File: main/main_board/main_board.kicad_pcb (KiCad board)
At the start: 4 copper layers, 426.7 x 242.2 mm, 58 parts, among them J7 SCKB, J8 SCKA, J9 MCLK, P2 my_pcie_8x, P3 my_pcie_8x, P4 my_pcie_8x, P5 my_pcie_8x, P6 my_pcie_8x, U11 MCP1755S-3302E/DB, U12 FIN1047, U13 DS90LV048, U14 74LVC541A, U15 FIN1047, U16 FIN1047, U17 FIN1047

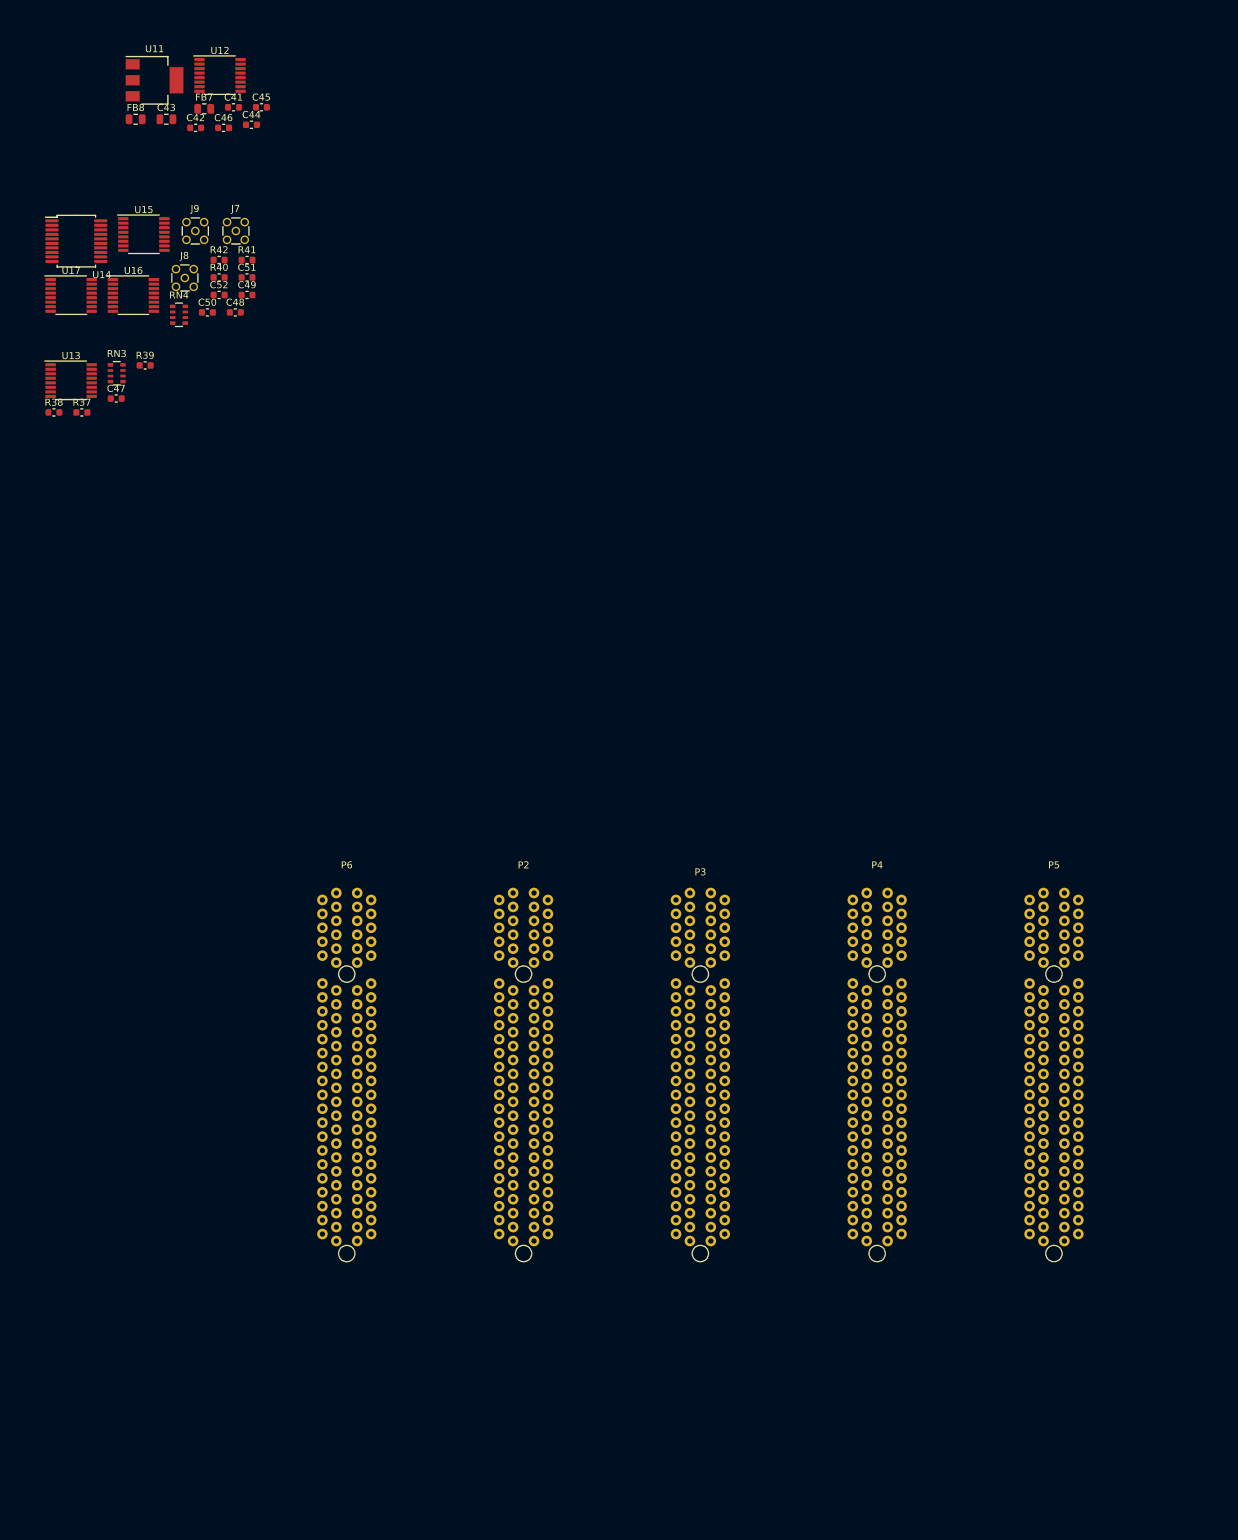
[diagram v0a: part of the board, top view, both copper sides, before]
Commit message: A bunch of thinking about RFI and ESD, and some testing.  Mostly reflected in notebook.txt. Also another more explicit round of consideration of box-level grounding and power distribution, because this affects the power conditioning on the main board.  Power nets on the main board are mostly captured.  I added supply decoupling at each plugin slot.
in_filter.sxsch: added simulation of ESD, use vendor models for TVS diode and ferrite.

power_budget.xlsx: get rid of sheets for the input boards not implemented.  Add sheet for
the main board and carry over data from the input board sheet.
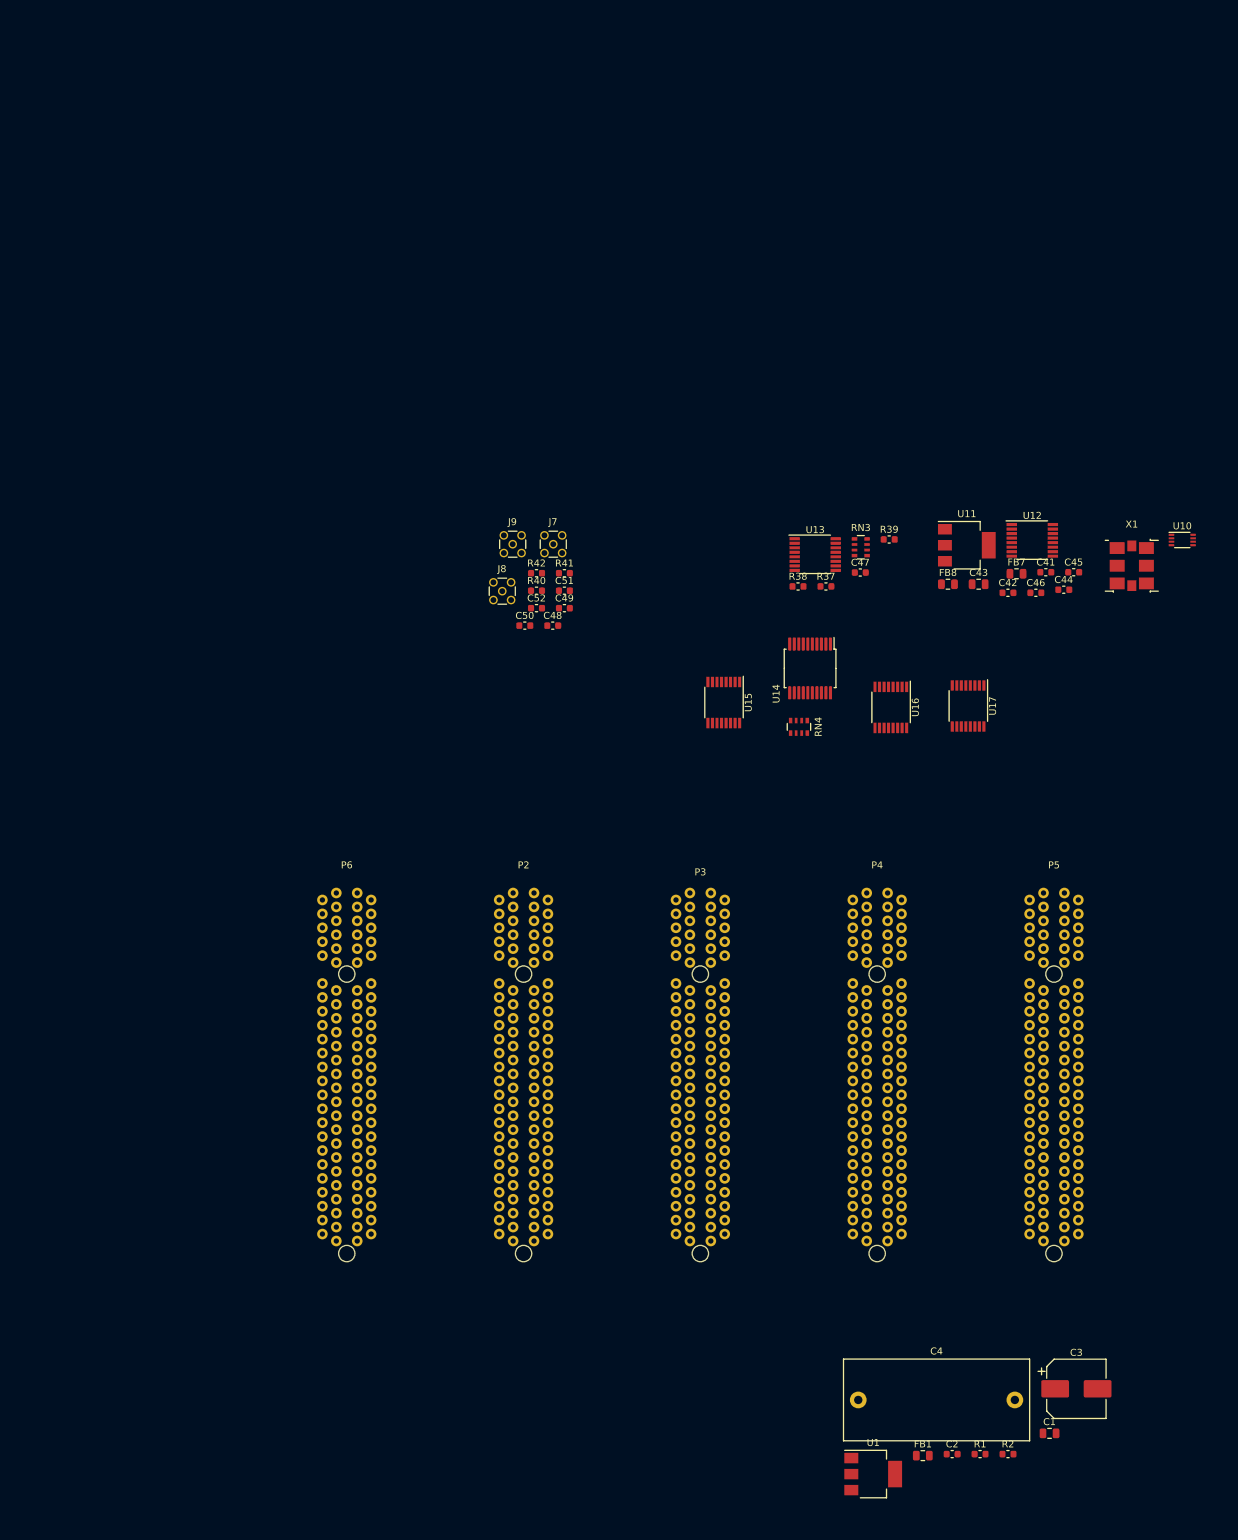
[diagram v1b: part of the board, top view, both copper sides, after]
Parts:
- added C1: 1uF, Capacitor_SMD:C_0805_2012Metric, F.Cu at (419.2, 243.0)
- added C2: 10uF, Capacitor_SMD:C_0603_1608Metric, F.Cu at (405.2, 246.0)
- added C3: 330uF, Capacitor_SMD:CP_Elec_8x6.7, F.Cu at (423.1, 236.6)
- added C4: 22 uF, Capacitor_THT:C_Rect_L26.5mm_W11.5mm_P22.50mm_MKS4, F.Cu at (391.7, 238.2)
- added FB1: 21 Ohm, Inductor_SMD:L_0805_2012Metric, F.Cu at (401.0, 246.2)
- added R1: 1K, Resistor_SMD:R_0603_1608Metric, F.Cu at (409.2, 246.0)
- added R2: 200, Resistor_SMD:R_0603_1608Metric, F.Cu at (413.2, 246.0)
- added U1: NCP1117STAT3G, Package_TO_SOT_SMD:SOT-223, F.Cu at (393.9, 248.8)
- added U10: 74AUP1G74, Package_SO:VSSOP-8_2.3x2mm_P0.5mm, F.Cu at (438.3, 114.7)
- added X1: Si570, input:QFN-8_5x7_Pitch2.54mm, F.Cu at (431.0, 118.3)
- moved U17 141.7 mm to (407.5, 138.5), turned to 270 degrees
- moved C41 134.5 mm to (418.7, 119.3)
- moved C42 134.5 mm to (413.2, 122.2)
- moved U12 134.5 mm to (416.7, 114.7)
- moved C43 134.5 mm to (409.0, 121.0)
- moved C44 134.5 mm to (421.2, 121.8)
- moved C45 134.5 mm to (422.7, 119.3)
- moved C46 134.5 mm to (417.2, 122.2)
- moved FB7 134.5 mm to (414.5, 119.5)
- moved FB8 134.5 mm to (404.6, 121.0)
- moved U11 134.5 mm to (407.3, 115.4)
- moved U16 123.9 mm to (396.4, 138.7), turned to 270 degrees
- moved U14 122.0 mm to (384.8, 133.1), turned to 270 degrees
- moved R39 109.8 mm to (396.2, 114.6)
- moved U13 109.8 mm to (385.5, 116.7)
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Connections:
- net /output_slot/MCLK+ renamed DOUT2+
- net /output_slot/MCLK- renamed DOUT2-
- net /output_slot/SCKA+ renamed DOUT1+
- net /output_slot/SCKA- renamed DOUT1-
- net /output_slot/SCKB+ renamed /output_slot/SYSCLK+
- net /output_slot/SCKB- renamed /output_slot/SYSCLK-
- net /output_slot/SDOA1+ renamed DFB1+
- net /output_slot/SDOA1- renamed DFB1-
- net /output_slot/SDOA2+ renamed DFB3+
- net /output_slot/SDOA2- renamed DFB3-
- net /output_slot/SDOA3+ renamed DFB4+
- net /output_slot/SDOA3- renamed DFB4-
- net /output_slot/SDOB1+ renamed DFB2+
- net /output_slot/SDOB1- renamed DFB2-
- net Net-(P6-PadA3) renamed DOUTL1
- net Net-(P6-PadA7) renamed DOUTL3
- net Net-(P6-PadA8) renamed DOUTL5
- net Net-(P6-PadB25) renamed DOUT3-
- net Net-(P6-PadB3) renamed DOUTL2
- net Net-(P6-PadB7) renamed LDOUT4
- net Net-(P6-PadB8) renamed DOUTL6
- P6 pad A25: Net-(P6-PadA25) -> GND
- P6 pad A26: GND -> DOUT4+
- P6 pad A27: Net-(P6-PadA27) -> DOUT4-
- P6 pad A30: GNDA -> DOUT5+
- P6 pad A31: GNDA -> DOUT5-
- P6 pad A34: GNDA -> DOUT7+
- P6 pad A35: GNDA -> DOUT7-
- P6 pad A36: +5VANA -> GNDA
- P6 pad A37: +10V -> GNDA
- P6 pad A38: +10V -> GNDA
- P6 pad A39: -6V -> GNDA
- P6 pad A40: -6V -> GNDA
- P6 pad A41: GNDA -> +5VANA
- P6 pad A42: VREF+ -> +10V
- P6 pad A43: VREF- -> -6V
- P6 pad A45: Net-(P6-PadA45) -> VREF+
- P6 pad A46: Net-(P6-PadA46) -> VREF-
- P6 pad B24: GND -> DOUT3+
- P6 pad B27: Net-(P6-PadB27) -> GND
- P6 pad B28: GND -> DOUT4+
- P6 pad B29: GNDA -> DOUT4-
- P6 pad B32: GNDA -> DOUT6+
- P6 pad B33: GNDA -> DOUT6-
- P6 pad B36: +5VANA -> DOUT8+
- P6 pad B37: +10V -> DOUT8-
- P6 pad B38: +10V -> GNDA
- P6 pad B39: -6V -> GNDA
- P6 pad B40: -6V -> GNDA
- P6 pad B41: GNDA -> +5VANA
- P6 pad B42: GNDA -> +10V
- P6 pad B43: GNDA -> -6V
- P6 pad B45: Net-(P6-PadB45) -> GNDA
- P6 pad B46: Net-(P6-PadB46) -> GNDA
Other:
- board text added: "Microzed footprint"

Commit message: Mostly work on hooking in the Microzed using kipart symbols and a footprint. Also added 2.5V VCCIO regulator.
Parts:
- added C1: 1uF, Capacitor_SMD:C_0805_2012Metric, F.Cu at (369.9, 236.5)
- added C10: 1uF, Capacitor_SMD:C_0805_2012Metric, F.Cu at (262.7, 65.6)
- added C11: 1uF, Capacitor_SMD:C_0805_2012Metric, F.Cu at (279.1, 81.1)
- added C12: 330uF, Capacitor_SMD:CP_Elec_8x6.7, F.Cu at (338.5, 150.8)
- added C13: 330uF, Capacitor_SMD:CP_Elec_8x6.7, F.Cu at (321.5, 151.4)
- added C14: 1uF, Capacitor_SMD:C_0805_2012Metric, F.Cu at (279.7, 84.0)
- added C15: 1uF, Capacitor_SMD:C_0805_2012Metric, F.Cu at (279.1, 78.1)
- added C16: 1uF, Capacitor_SMD:C_0805_2012Metric, F.Cu at (275.3, 85.0)
- added C17: 1uF, Capacitor_SMD:C_0805_2012Metric, F.Cu at (279.1, 75.2)
- added C18: 1uF, Capacitor_SMD:C_0805_2012Metric, F.Cu at (275.3, 88.0)
- added C19: 330uF, Capacitor_SMD:CP_Elec_8x6.7, F.Cu at (327.7, 51.6)
- added C2: 1uF, Capacitor_SMD:C_0805_2012Metric, F.Cu at (341.3, 251.6)
- added C20: 330uF, Capacitor_SMD:CP_Elec_8x6.7, F.Cu at (321.1, 137.4)
- added C21: 330uF, Capacitor_SMD:CP_Elec_8x6.7, F.Cu at (354.9, 150.9)
- added C22: 10uF, Capacitor_SMD:C_0603_1608Metric, F.Cu at (305.1, 77.6)
- added C23: 10uF, Capacitor_SMD:C_0603_1608Metric, F.Cu at (307.7, 72.5)
- added C24: 1uF, Capacitor_SMD:C_0805_2012Metric, F.Cu at (340.9, 223.7)
- added C25: 1uF, Capacitor_SMD:C_0805_2012Metric, F.Cu at (345.3, 223.7)
- added C26: 1uF, Capacitor_SMD:C_0805_2012Metric, F.Cu at (345.3, 226.7)
- added C27: 1uF, Capacitor_SMD:C_0805_2012Metric, F.Cu at (340.9, 226.7)
- added C28: 1uF, Capacitor_SMD:C_0805_2012Metric, F.Cu at (371.6, 227.7)
- added C29: 1uF, Capacitor_SMD:C_0805_2012Metric, F.Cu at (371.6, 224.7)
- added C3: bulk >=16V, Capacitor_SMD:C_1210_3225Metric, F.Cu at (364.9, 237.1)
- added C30: 1uF, Capacitor_SMD:C_0805_2012Metric, F.Cu at (367.2, 227.7)
- added C31: 1uF, Capacitor_SMD:C_0805_2012Metric, F.Cu at (367.2, 224.7)
- added C32: 1uF, Capacitor_SMD:C_0805_2012Metric, F.Cu at (392.8, 228.2)
- added C33: 1uF, Capacitor_SMD:C_0805_2012Metric, F.Cu at (392.8, 225.2)
- added C34: 1uF, Capacitor_SMD:C_0805_2012Metric, F.Cu at (388.3, 228.2)
- added C35: 1uF, Capacitor_SMD:C_0805_2012Metric, F.Cu at (388.3, 225.2)
- added C36: 1uF, Capacitor_SMD:C_0805_2012Metric, F.Cu at (423.0, 227.9)
- added C37: 1uF, Capacitor_SMD:C_0805_2012Metric, F.Cu at (423.0, 225.0)
- added C38: 1uF, Capacitor_SMD:C_0805_2012Metric, F.Cu at (418.6, 227.9)
- added C39: 1uF, Capacitor_SMD:C_0805_2012Metric, F.Cu at (418.6, 225.0)
- added C40: 1uF, Capacitor_SMD:C_0805_2012Metric, F.Cu at (315.3, 226.3)
- added C43: 1uF, Capacitor_SMD:C_0805_2012Metric, F.Cu at (319.7, 223.4)
- added C45: 1uF, Capacitor_SMD:C_0805_2012Metric, F.Cu at (315.3, 223.4)
- added C47: 1uF, Capacitor_SMD:C_0805_2012Metric, F.Cu at (306.6, 84.4)
- added C5: 3.3 uF, Capacitor_THT:C_Rect_L13.0mm_W6.0mm_P10.00mm_FKS3_FKP3_MKS4, F.Cu at (341.4, 246.3)
- added C53: 1uF, Capacitor_SMD:C_0805_2012Metric, F.Cu at (319.7, 226.3)
- added C54: 100nF, Capacitor_SMD:C_0603_1608Metric, F.Cu at (454.0, 141.3)
- added C55: 10uF, Capacitor_SMD:C_0603_1608Metric, F.Cu at (328.3, 67.1)
- added C56: 10uF, Capacitor_SMD:C_0603_1608Metric, F.Cu at (330.5, 73.9)
- added C6: 47uF, Capacitor_SMD:C_1210_3225Metric, F.Cu at (356.4, 250.0)
- added C7: 1uF, Capacitor_SMD:C_0805_2012Metric, F.Cu at (350.1, 251.6)
- added C8: OPT, Capacitor_SMD:C_0603_1608Metric, F.Cu at (364.1, 244.7)
- added C9: 47uF, Capacitor_SMD:C_1210_3225Metric, F.Cu at (364.9, 241.3)
- added D1: 10V (standoff), Diode_SMD:D_SMA, F.Cu at (262.2, 76.2)
- added D2: 10V (standoff), Diode_SMD:D_SMA, F.Cu at (272.4, 69.7)
- added D3: 5V (standoff), Diode_SMD:D_SMA, F.Cu at (262.5, 82.9)
- added FB2: 2K Ohm, Inductor_SMD:L_0805_2012Metric, F.Cu at (369.9, 239.4)
- added FB3: 1.2 A, Inductor_SMD:L_0805_2012Metric, F.Cu at (272.5, 61.4)
- added J1: Conn_02x08_Odd_Even, Connector_PinHeader_2.54mm:PinHeader_2x08_P2.54mm_Vertical, F.Cu at (248.6, 71.6)
- added J2: MCLK, Connector_Coaxial:MMCX_Molex_73415-1471_Vertical, F.Cu at (429.7, 129.7)
- added R1: 10, Resistor_SMD:R_0603_1608Metric, F.Cu at (365.3, 249.7)
- added R10: 100, Resistor_SMD:R_0603_1608Metric, F.Cu at (449.8, 146.1)
- added R11: 100, Resistor_SMD:R_0603_1608Metric, F.Cu at (440.9, 148.1)
- added R2: 10, Resistor_SMD:R_0603_1608Metric, F.Cu at (365.3, 247.2)
- added R3: 40K, Resistor_SMD:R_0603_1608Metric, F.Cu at (368.1, 244.7)
- added R4: 10, Resistor_SMD:R_0603_1608Metric, F.Cu at (361.2, 251.7)
- added R5: 0, Resistor_SMD:R_0603_1608Metric, F.Cu at (369.7, 242.2)
- added R6: 0, Resistor_SMD:R_0603_1608Metric, F.Cu at (361.2, 249.2)
- added R7: 1K, Resistor_SMD:R_0603_1608Metric, F.Cu at (434.6, 130.6)
- added R8: 33, Resistor_SMD:R_0603_1608Metric, F.Cu at (434.6, 128.1)
- added R9: 100, Resistor_SMD:R_0603_1608Metric, F.Cu at (444.9, 148.1)
- added RN1: 33, Resistor_SMD:R_Array_Convex_4x0603, F.Cu at (449.9, 142.4)
- added U2: OPA209, Package_SO:SOIC-8_3.9x4.9mm_P1.27mm, F.Cu at (357.9, 244.7)
- added U3: MCP1755S-3302E/DB, Package_TO_SOT_SMD:SOT-223-3_TabPin2, F.Cu at (294.9, 74.4)
- added U4: MCP1755S-3302E/DB, Package_TO_SOT_SMD:SOT-223-3_TabPin2, F.Cu at (295.5, 85.9)
- added U5: DS90LV048, Package_SO:TSSOP-16_4.4x5mm_P0.65mm, F.Cu at (443.3, 143.5)
- added U6: AP3761C-25SP, Package_SO:SOIC-8-1EP_3.9x4.9mm_P1.27mm_EP2.41x3.3mm_ThermalVias, F.Cu at (330.5, 62.6)
- added X1: MicroZed, main_board:Microzed, F.Cu at (391.5, 72.4)
- C4: value 22 uF -> 3.3 uF; footprint Capacitor_THT:C_Rect_L26.5mm_W11.5mm_P22.50mm_MKS4 -> Capacitor_THT:C_Rect_L13.0mm_W6.0mm_P10.00mm_FKS3_FKP3_MKS4
- FB1: value 21 Ohm -> 2K Ohm
- U1: value NCP1117STAT3G -> MAX6220ASA-5.0+; footprint Package_TO_SOT_SMD:SOT-223 -> Package_SO:SOIC-8_3.9x4.9mm_P1.27mm
- moved FB1 55.6 mm to (345.7, 251.6)
- moved C4 50.4 mm to (341.4, 238.8)
- moved U1 37.5 mm to (357.9, 238.2)
- renumbered X1 to X2
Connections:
- net FPGA_SYNC renamed Net-(U14-Pad6)
- net OUT_CLK+ renamed OUT_SYSCLK+
- net OUT_CLK- renamed OUT_SYSCLK-
- C4 pad 2: Net-(C4-Pad2) -> VREF-
- C44 pad 1: VCC -> +3V3_CLOCK
- C46 pad 1: VCC -> +3V3_CLOCK
- FB7 pad 1: VCC -> +3V3_CLOCK
- P2 pad A29: GNDA -> VREF-
- P2 pad A3: CARDSEL0 -> /input_slots/card_slot0/CARDSEL
- P2 pad A30: GNDA -> VREF-
- P2 pad A31: GNDA -> VREF-
- P2 pad A32: GNDA -> VREF-
- P2 pad A33: GNDA -> VREF-
- P2 pad A34: GNDA -> VREF-
- P2 pad A35: GNDA -> VREF-
- P2 pad A41: GNDA -> VREF-
- P2 pad A44: GNDA -> VREF-
- P2 pad A47: GNDA -> VREF-
- P2 pad B29: GNDA -> VREF-
- P2 pad B30: GNDA -> VREF-
- P2 pad B31: GNDA -> VREF-
- P2 pad B32: GNDA -> VREF-
- P2 pad B33: GNDA -> VREF-
- P2 pad B34: GNDA -> VREF-
- P2 pad B35: GNDA -> VREF-
- P2 pad B41: GNDA -> VREF-
- P2 pad B42: GNDA -> VREF-
- P2 pad B43: GNDA -> VREF-
- P2 pad B44: GNDA -> VREF-
- P2 pad B47: GNDA -> VREF-
- P3 pad A29: GNDA -> VREF-
- P3 pad A3: CARDSEL1 -> /input_slots/card_slot1/CARDSEL
- P3 pad A30: GNDA -> VREF-
- P3 pad A31: GNDA -> VREF-
- P3 pad A32: GNDA -> VREF-
- P3 pad A33: GNDA -> VREF-
- P3 pad A34: GNDA -> VREF-
- P3 pad A35: GNDA -> VREF-
- P3 pad A41: GNDA -> VREF-
- P3 pad A44: GNDA -> VREF-
- P3 pad A47: GNDA -> VREF-
- P3 pad B29: GNDA -> VREF-
- P3 pad B30: GNDA -> VREF-
- P3 pad B31: GNDA -> VREF-
- P3 pad B32: GNDA -> VREF-
- P3 pad B33: GNDA -> VREF-
- P3 pad B34: GNDA -> VREF-
- P3 pad B35: GNDA -> VREF-
- P3 pad B41: GNDA -> VREF-
- P3 pad B42: GNDA -> VREF-
- P3 pad B43: GNDA -> VREF-
- P3 pad B44: GNDA -> VREF-
- P3 pad B47: GNDA -> VREF-
- P4 pad A29: GNDA -> VREF-
- P4 pad A3: CARDSEL2 -> /input_slots/card_slot2/CARDSEL
- P4 pad A30: GNDA -> VREF-
- P4 pad A31: GNDA -> VREF-
- P4 pad A32: GNDA -> VREF-
- P4 pad A33: GNDA -> VREF-
- P4 pad A34: GNDA -> VREF-
- P4 pad A35: GNDA -> VREF-
- P4 pad A41: GNDA -> VREF-
- P4 pad A44: GNDA -> VREF-
- P4 pad A47: GNDA -> VREF-
- P4 pad B29: GNDA -> VREF-
- P4 pad B30: GNDA -> VREF-
- P4 pad B31: GNDA -> VREF-
- P4 pad B32: GNDA -> VREF-
- P4 pad B33: GNDA -> VREF-
- P4 pad B34: GNDA -> VREF-
- P4 pad B35: GNDA -> VREF-
- P4 pad B41: GNDA -> VREF-
- P4 pad B42: GNDA -> VREF-
- P4 pad B43: GNDA -> VREF-
- P4 pad B44: GNDA -> VREF-
- P4 pad B47: GNDA -> VREF-
- P5 pad A29: GNDA -> VREF-
- P5 pad A3: CARDSEL3 -> /input_slots/card_slot3/CARDSEL
- P5 pad A30: GNDA -> VREF-
- P5 pad A31: GNDA -> VREF-
- P5 pad A32: GNDA -> VREF-
- P5 pad A33: GNDA -> VREF-
- P5 pad A34: GNDA -> VREF-
- P5 pad A35: GNDA -> VREF-
- P5 pad A41: GNDA -> VREF-
- P5 pad A44: GNDA -> VREF-
- P5 pad A47: GNDA -> VREF-
- P5 pad B29: GNDA -> VREF-
- P5 pad B30: GNDA -> VREF-
- P5 pad B31: GNDA -> VREF-
- P5 pad B32: GNDA -> VREF-
- P5 pad B33: GNDA -> VREF-
- P5 pad B34: GNDA -> VREF-
- P5 pad B35: GNDA -> VREF-
- P5 pad B41: GNDA -> VREF-
- P5 pad B42: GNDA -> VREF-
- P5 pad B43: GNDA -> VREF-
- P5 pad B44: GNDA -> VREF-
- P5 pad B47: GNDA -> VREF-
- P6 pad A29: GNDA -> VREF-
- P6 pad A32: GNDA -> VREF-
- P6 pad A33: GNDA -> VREF-
- P6 pad A36: GNDA -> VREF-
- P6 pad A37: GNDA -> VREF-
- P6 pad A38: GNDA -> VREF-
- P6 pad A39: GNDA -> VREF-
- P6 pad A40: GNDA -> VREF-
- P6 pad A44: GNDA -> VREF-
- P6 pad A47: GNDA -> VREF-
- P6 pad B30: GNDA -> VREF-
- P6 pad B31: GNDA -> VREF-
- P6 pad B34: GNDA -> VREF-
- P6 pad B35: GNDA -> VREF-
- P6 pad B38: GNDA -> VREF-
- P6 pad B39: GNDA -> VREF-
- P6 pad B40: GNDA -> VREF-
- P6 pad B44: GNDA -> VREF-
- P6 pad B45: GNDA -> VREF-
- P6 pad B46: GNDA -> VREF-
- P6 pad B47: GNDA -> VREF-
- U1 pad 1: Net-(C2-Pad1) -> (no net)
- U1 pad 3: Net-(C1-Pad2) -> Net-(C4-Pad1)
- U1 pad 4: Net-(C3-Pad1) -> VREF-
- U10 pad 2: VCC -> +3V3_CLOCK
- U10 pad 5: MCLK -> Net-(R7-Pad1)
- U10 pad 7: VCC -> +3V3_CLOCK
- U10 pad 8: VCC -> +3V3_CLOCK
- U12 pad 11: FPGA_CLK+ -> FPGA_SYSCLK+
- U12 pad 12: FPGA_CLK- -> FPGA_SYSCLK-
- U12 pad 4: VCC -> +3V3_CLOCK
- U15 pad 2: SCKA -> Net-(RN1-Pad6)
- U15 pad 3: SCKA -> Net-(RN1-Pad6)
- U15 pad 6: SCKA -> Net-(RN1-Pad6)
- U15 pad 7: SCKA -> Net-(RN1-Pad6)
- U16 pad 2: SCKB -> Net-(RN1-Pad5)
- U16 pad 3: SCKB -> Net-(RN1-Pad5)
- U16 pad 6: SCKB -> Net-(RN1-Pad5)
- U16 pad 7: SCKB -> Net-(RN1-Pad5)

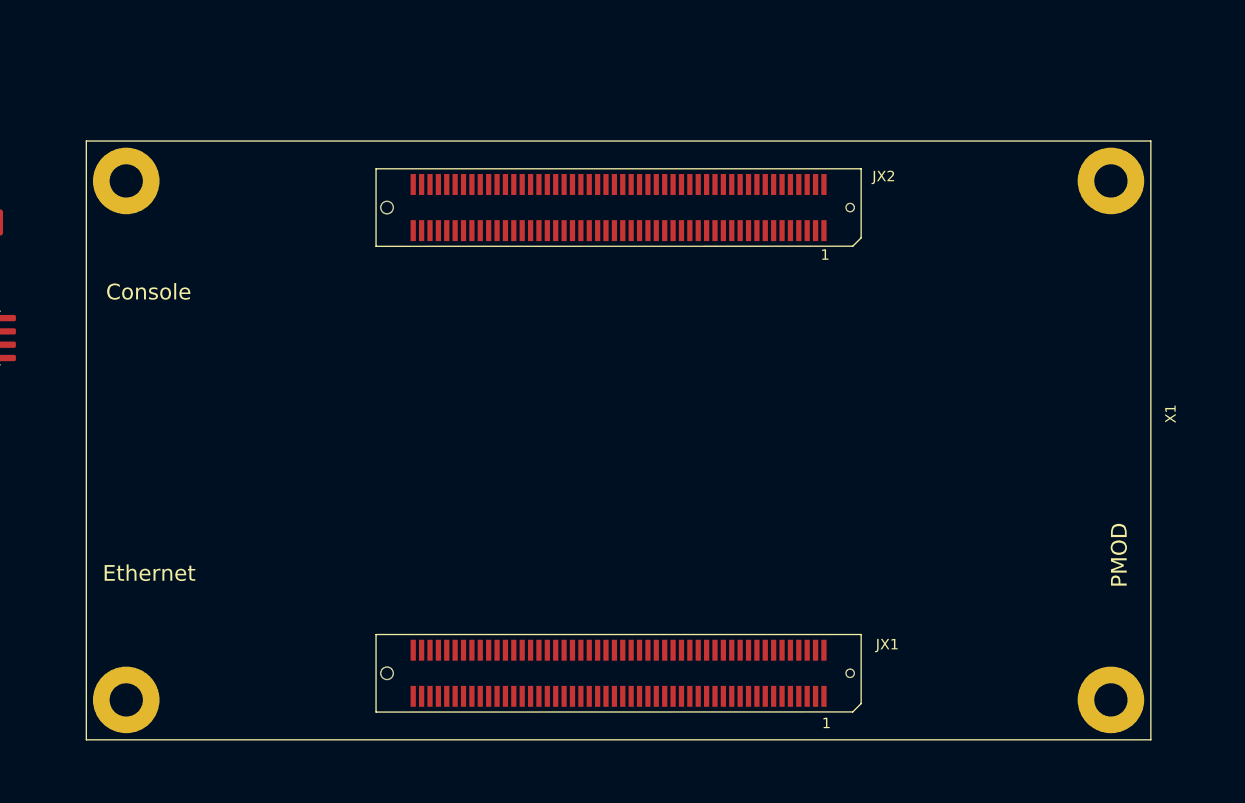
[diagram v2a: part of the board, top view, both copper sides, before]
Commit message: Updated for new microzed pin mapping scheme.
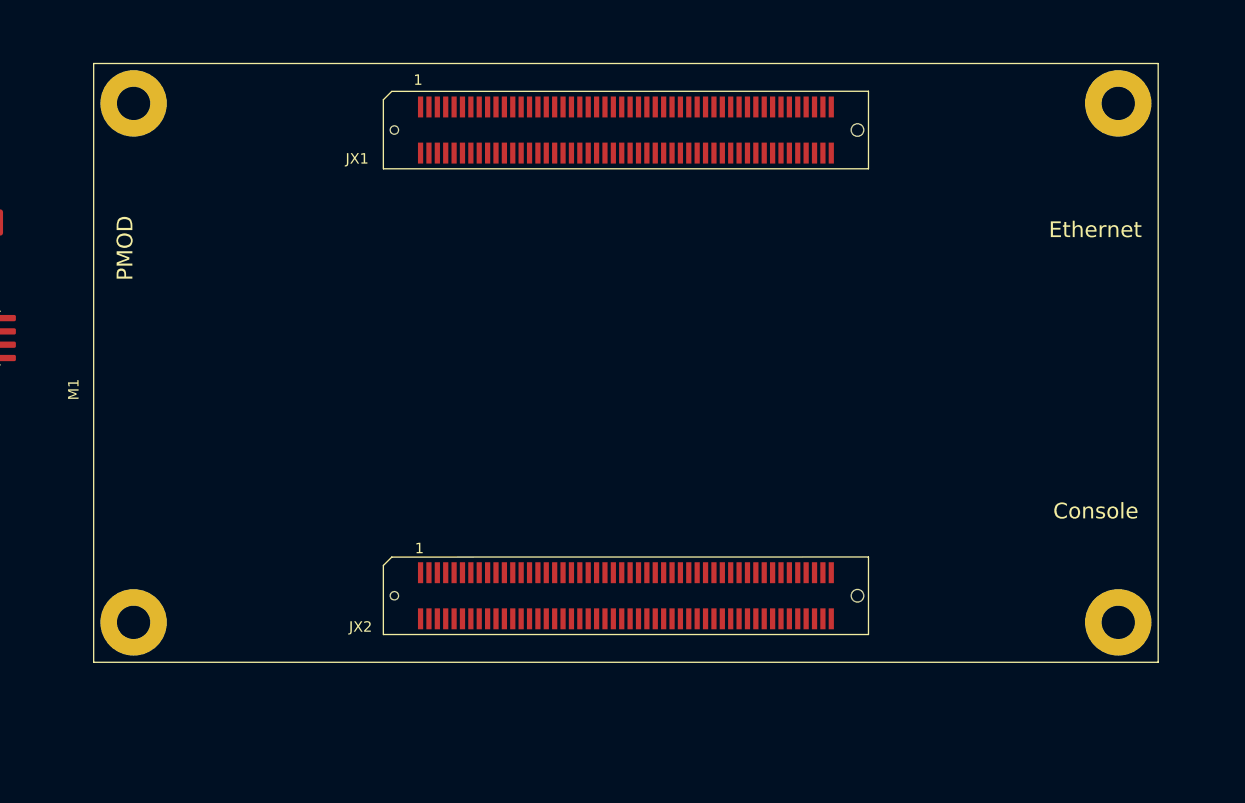
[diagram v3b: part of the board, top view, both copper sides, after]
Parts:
- removed X1: MicroZed, main_board:Microzed
- added M1: microzed, main_board:Microzed, F.Cu at (392.2, 65.0)
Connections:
- P6 pad A18: /output_slot/SYSCLK+ -> OUT_SYSCLK+
- P6 pad A19: /output_slot/SYSCLK- -> OUT_SYSCLK-
- P6 pad B28: DOUT4+ -> Net-(P6-PadB28)
- P6 pad B29: DOUT4- -> Net-(P6-PadB29)
- P6 pad B7: LDOUT4 -> DOUTL4
